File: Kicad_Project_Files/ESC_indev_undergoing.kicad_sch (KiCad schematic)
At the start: 0 parts

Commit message: updated schematic
added ir2110 circuitry , 1 cap leftover , tps connections left(maybe can switch over),
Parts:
- added C1, C2, C3: C, symbol Device:C
- added D1, D2, D3: 1N4001, Diode_THT:D_DO-41_SOD81_P10.16mm_Horizontal, symbol Diode:1N4001
- added R1: R_US, symbol Device:R_US
- added SW1: SW_Push, symbol Switch:SW_Push
- added U1: TPS560430X3FDBVR, TPS560430X3FDBVR:IC_TPS560430X3FDBVR, symbol TPS560430X3FDBVR:TPS560430X3FDBVR
- added U2, U3, U4: IR2110, Package_DIP:DIP-14_W7.62mm, symbol Driver_FET:IR2110
- added U5: ESP32-WROOM-32E, RF_Module:ESP32-WROOM-32E, symbol RF_Module:ESP32-WROOM-32E
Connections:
- new net: C2.1, D2.1 (K), U3.6 (VB)
- new net: R1.1, SW1.2, U5.3 (EN)
- new net: C3.1, D3.1 (K), U4.6 (VB)
- new net: C3.2, U4.5 (VS)
- new net: C2.2, U3.5 (VS)
- new net: C1.1, D1.1 (K), U2.6 (VB)
- new net: C1.2, U2.5 (VS)
- new net +15V: D1.2 (A), D2.2 (A), D3.2 (A), U2.3 (VCC), U3.3 (VCC), U4.3 (VCC)
- new net +5V: R1.2, U2.9 (VDD), U3.9 (VDD), U4.9 (VDD), U5.2 (VDD)
- new net GND: SW1.1, U2.11 (SD), U2.13 (VSS), U2.2 (COM), U3.11 (SD), U3.13 (VSS), U3.2 (COM), U4.11 (SD), U4.13 (VSS), U4.2 (COM), U5.[1,15,38,39] (GND)
- new net HIN1: U2.10 (HIN), U5.10 (IO25)
- new net HIN2: U3.10 (HIN)
- new net HIN3: U4.10 (HIN)
- new net HO1: U2.7 (HO)
- new net HO2: U3.7 (HO)
- new net HO3: U4.7 (HO)
- new net LIN1: U2.12 (LIN)
- new net LIN2: U3.12 (LIN)
- new net LIN3: U4.12 (LIN)
- new net LO1: U2.1 (LO)
- new net LO2: U3.1 (LO)
- new net LO3: U4.1 (LO)

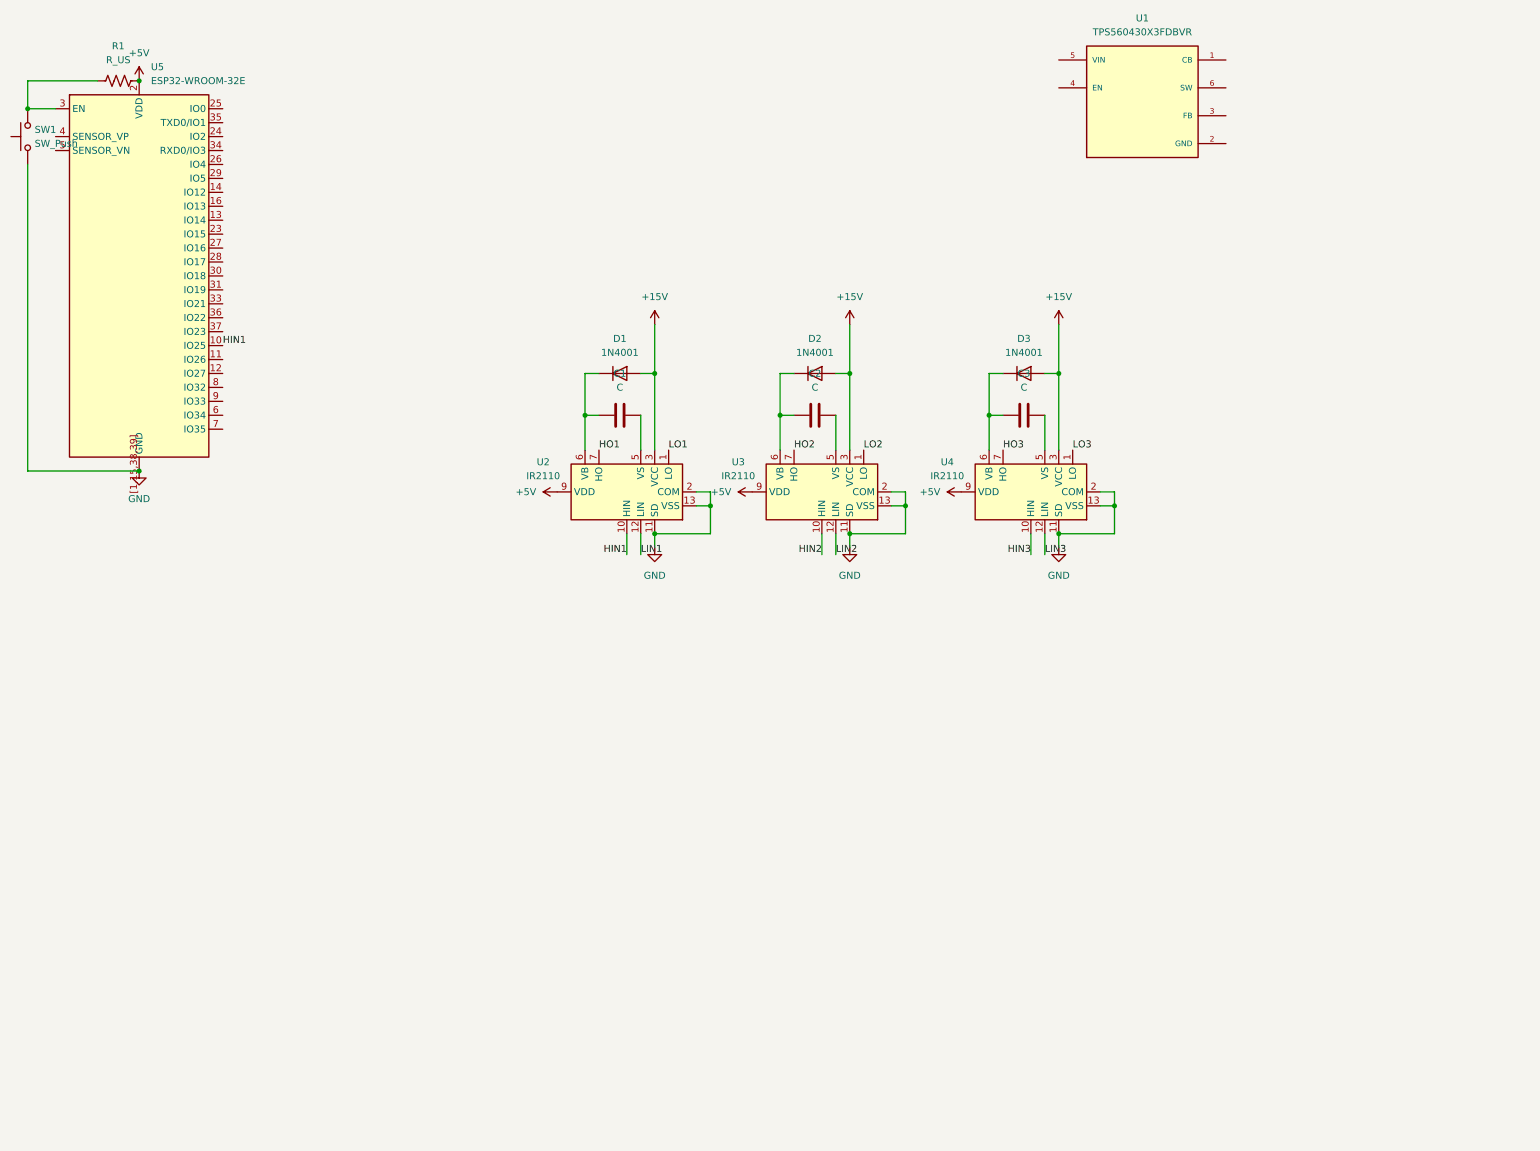
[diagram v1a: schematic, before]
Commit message: added 3 phase inverter circuitry
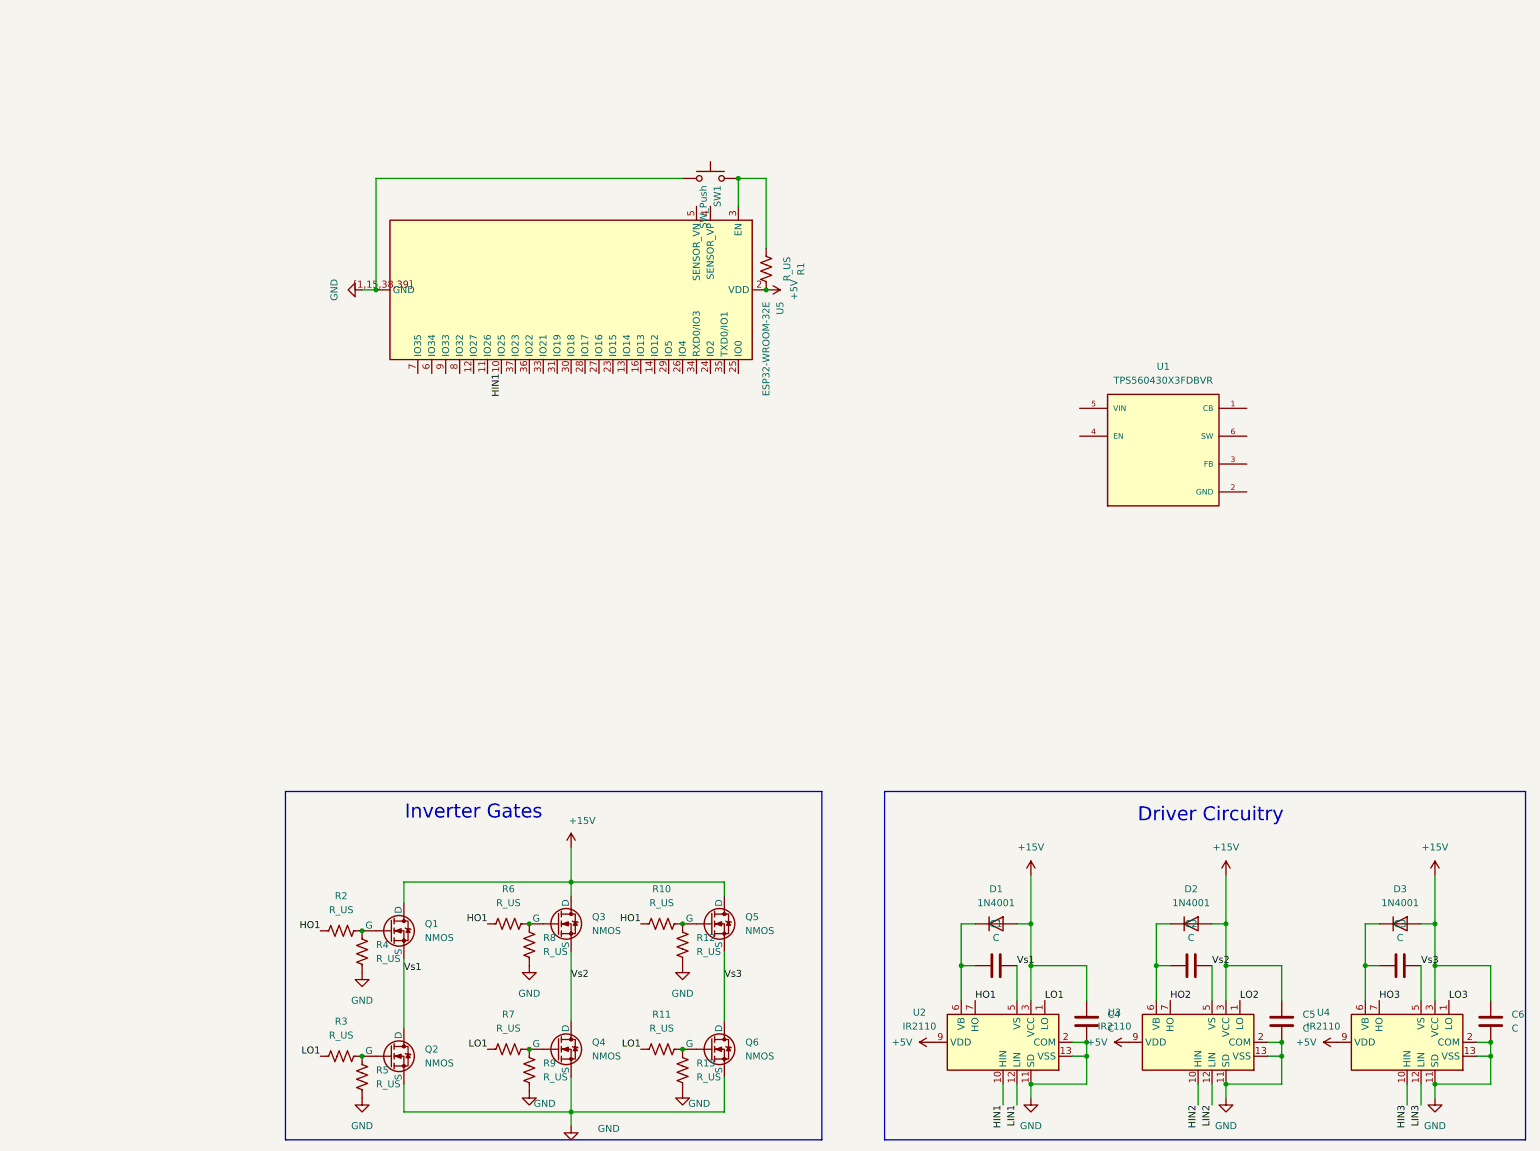
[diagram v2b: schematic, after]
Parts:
- added C4, C5, C6: C, symbol Device:C
- added Q1, Q2, Q3, Q4, Q5, Q6: NMOS, symbol Simulation_SPICE:NMOS
- added R10, R11, R12, R13, R2, R3, R4, R5, R6, R7, R8, R9: R_US, symbol Device:R_US
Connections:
- net +15V: now also C4.1, C5.1, C6.1, Q1.1 (D), Q3.1 (D), Q5.1 (D)
- net GND: now also C4.2, C5.2, C6.2, Q2.3 (S), Q4.3 (S), Q6.3 (S), R12.1, R13.1, R4.1, R5.1, R8.1, R9.1
- net HO1: now also R10.1, R2.1, R6.1
- net LO1: now also R11.1, R3.1, R7.1
- net Vs3: now reaches C3.2, U4.5 (VS)
- net Vs3: now also Q5.3 (S), Q6.1 (D)
- net Vs2: now reaches C2.2, U3.5 (VS)
- net Vs2: now also Q3.3 (S), Q4.1 (D)
- net Vs1: now reaches C1.2, U2.5 (VS)
- net Vs1: now also Q1.3 (S), Q2.1 (D)
- new net: Q6.2 (G), R11.2, R13.2
- new net: Q4.2 (G), R7.2, R9.2
- new net: Q3.2 (G), R6.2, R8.2
- new net: Q5.2 (G), R10.2, R12.2
- new net: Q1.2 (G), R2.2, R4.2
- new net: Q2.2 (G), R3.2, R5.2
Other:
- note added: "Driver Circuitry"
- note added: "Inverter Gates"
- moved on the sheet: C1, C2, C3, D1, D2, D3, R1, SW1, U1, U2, U3, U4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

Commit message: added circuitry for buck converter
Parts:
- added C7, C8, C9: C, symbol Device:C
- added L1: L, symbol Device:L
- added R14, R15: R_US, symbol Device:R_US
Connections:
- net +15V: now also U1.4 (EN), U1.5 (VIN), C7.1
- net GND: now also U1.2 (GND), C7.2, C9.2, R15.2
- net at U1.1 (CB): now also C8.1
- net at U1.3 (FB): now also R14.2, R15.1
- net at U1.6 (SW): now also C8.2, L1.1
- net +5V renamed +3.3V
- net +3.3V: now also C9.1, L1.2, R14.1; no longer U4.9 (VDD)
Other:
- note added: "Power Converter"
- moved on the sheet: U1

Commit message: assined foorprints , added libraries from official ki cad
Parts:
- added J1: XT60-M, Connector_AMASS:AMASS_XT60PW-M_1x02_P7.20mm_Horizontal, symbol XT60-M:XT60-M
- C1, C2, C3, C4, C5, C6, C7: footprint (none) -> Capacitor_SMD:C_1206_3216Metric
- C8: footprint (none) -> Capacitor_SMD:C_0805_2012Metric
- C9: footprint (none) -> Capacitor_SMD:C_0805_2012Metric_Pad1.18x1.45mm_HandSolder
- L1: footprint (none) -> Inductor_SMD:L_6.3x6.3_H3
- Q1, Q2, Q3, Q4, Q5, Q6: footprint (none) -> PCM_Package_TO_SOT_THT_AKL:TO-220-3_Horizontal_TabDown
- R1, R10, R11, R12, R13, R14, R15, R2, R3, R4, R5, R6, R7, R8, R9: footprint (none) -> PCM_Resistor_SMD_AKL:R_1206_3216Metric
- SW1: footprint (none) -> Button_Switch_SMD:SW_Push_1P1T_NO_CK_KMR2
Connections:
- net +15V: now also J1.N (NEG)
- net GND: now also J1.P (POS)
- net HO1: no longer R10.1, R6.1
- net HO2: now also R6.1
- net HO3: now also R10.1
- net LO1: no longer R11.1, R7.1
- net LO2: now also R7.1
- net LO3: now also R11.1
- no-connect marks 0 -> 15

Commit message: major pcb desgin advance
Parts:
- removed J1: XT60-M, Connector_AMASS:AMASS_XT60PW-M_1x02_P7.20mm_Horizontal, symbol XT60-M:XT60-M
- removed U2, U3, U4: IR2110, Package_DIP:DIP-14_W7.62mm, symbol Driver_FET:IR2110
- added D4: LED, LED_SMD:LED_0603_1608Metric_Pad1.05x0.95mm_HandSolder, symbol Device:LED
- added J2, J3: JST_PH_1x04_P2mm, PCM_fab:Header_JST_PH_1x04_P2mm_Vertical_SMD, symbol PCM_fab:Conn_Header_JST_PH_1x04_P2mm_Vertical_SMD
- added R16, R17, R19, R21, R22, R24: 33k, PCM_Resistor_SMD_AKL:R_0603_1608Metric_Pad1.05x0.95mm_HandSolder, symbol Device:R_US
- added R18, R20, R23, R25: 10k, PCM_Resistor_SMD_AKL:R_0603_1608Metric_Pad1.05x0.95mm_HandSolder, symbol Device:R_US
- added SW2: SW_Push, Button_Switch_SMD:SW_Push_1P1T_NO_CK_KMR2, symbol Switch:SW_Push
- added U10, U6, U7, U8, U9: (no value), solderpads:Untitled, symbol solderpad_Library:solderpad_1
- added U11: LMV324, PCM_Package_SO_AKL:SSOP-14_5.3x6.2mm_P0.65mm, symbol Amplifier_Operational:LMV324
- added U2, U3, U4: IR2110S, Package_SO:SOIC-16W_7.5x10.3mm_P1.27mm, symbol Driver_FET:IR2110S
- C4, C5, C6: footprint Capacitor_SMD:C_1206_3216Metric -> Capacitor_SMD:C_0805_2012Metric
- D1, D2, D3: footprint Diode_THT:D_DO-41_SOD81_P10.16mm_Horizontal -> Diode_SMD:D_1206_3216Metric_Pad1.42x1.75mm_HandSolder
- Q1, Q2, Q3, Q4, Q5, Q6: footprint PCM_Package_TO_SOT_THT_AKL:TO-220-3_Horizontal_TabDown -> Kicad_Project_Files:TO-263-2
- R1, R10, R11, R14, R15, R2, R3, R6, R7: footprint PCM_Resistor_SMD_AKL:R_1206_3216Metric -> PCM_Resistor_SMD_AKL:R_0603_1608Metric_Pad1.05x0.95mm_HandSolder
- R12, R13, R4, R5, R8, R9: value R_US -> 10k; footprint PCM_Resistor_SMD_AKL:R_1206_3216Metric -> PCM_Resistor_SMD_AKL:R_0603_1608Metric_Pad1.05x0.95mm_HandSolder
- U1: footprint TPS560430X3FDBVR:IC_TPS560430X3FDBVR -> Kicad_Project_Files:IC_TPS560430X3FDBVR
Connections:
- net +3.3V: now also D4.2 (A), J2.4, J3.4, R25.2, U11.4 (V+), U2.11 (VDD), U3.11 (VDD), U4.11 (VDD)
- net GND: now also D4.1 (K), J2.1, J3.1, R18.1, R20.1, R23.1, SW2.1, U10., U11.11 (V-), U2.13 (SD), U2.15 (VSS), U2.2 (COM), U3.13 (SD), U3.15 (VSS), U3.2 (COM), U4.13 (SD), U4.15 (VSS), U4.2 (COM); no longer R12.1, R4.1, R8.1
- net HIN1: now also U2.12 (HIN)
- net HIN2: now also U3.12 (HIN)
- net HIN3: now also U4.12 (HIN)
- net HO1: now also U2.8 (HO)
- net HO2: now also U3.8 (HO)
- net HO3: now also U4.8 (HO)
- net LIN1: now also U2.14 (LIN)
- net LIN2: now also U3.14 (LIN)
- net LIN3: now also U4.14 (LIN)
- net LO1: now also U2.1 (LO)
- net LO2: now also U3.1 (LO)
- net LO3: now also U4.1 (LO)
- net at C2.1, D2.1 (K): now also U3.7 (VB)
- net at C3.1, D3.1 (K): now also U4.7 (VB)
- net at C1.1, D1.1 (K): now also U2.7 (VB)
- net at U5.25 (IO0): now also R25.1, SW2.2
- net at U5.33 (IO21): now also J3.3
- net at U5.34 (RXD0/IO3): now also J2.2
- net at U5.35 (TXD0/IO1): now also J2.3
- net at U5.36 (IO22): now also J3.2
- net +15V renamed 15v
- net 15v: now also U2.3 (VCC), U3.3 (VCC), U4.3 (VCC), U9.
- net Vs1 renamed P1
- net P1: now also R4.1, R17.2, U2.6 (VS), U6.
- net Vs2 renamed P2
- net P2: now also R8.1, R19.2, U3.6 (VS), U7.
- net Vs3 renamed P3
- net P3: now also R12.1, R22.2, U4.6 (VS), U8.
- new net: R16.1, R17.1, R18.2, U11.10 (+)
- new net: R16.2, R21.2, R24.2, U11.2 (-), U11.6 (-), U11.9 (-)
- new net: R19.1, R20.2, R21.1, U11.5 (+)
- new net: R22.1, R23.2, R24.1, U11.3 (+)
- no-connect marks 15 -> 17
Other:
- moved on the sheet: R1, SW1, U5

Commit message: added traces to drivers
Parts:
- added H1, H2, H3, H4: MountingHole_Pad, MountingHole:MountingHole_3.2mm_M3_DIN965_Pad, symbol Mechanical:MountingHole_Pad
- U11: footprint PCM_Package_SO_AKL:SSOP-14_5.3x6.2mm_P0.65mm -> PCM_Package_SO_AKL:SOIC-14_3.9x8.7mm_P1.27mm
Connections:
- net at U11.8: now also U5.8 (IO32)
- net at U11.7: now also U5.12 (IO27)
- net at U11.1: now also U5.11 (IO26)
- no-connect marks 17 -> 19
